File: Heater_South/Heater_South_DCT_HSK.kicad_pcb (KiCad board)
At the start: 2 copper layers, 52.1 x 57.1 mm, 8 parts, among them J1 NHB1, J2 NHB2, J3 Heater North

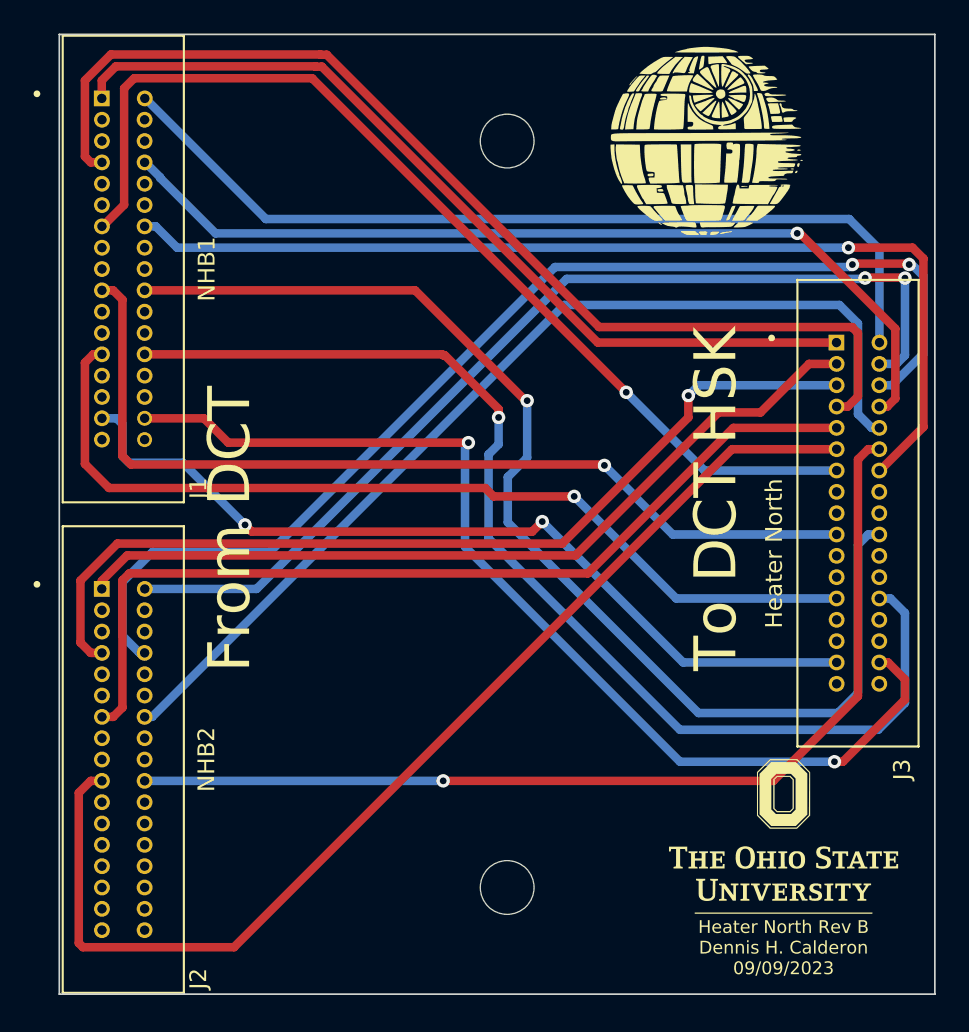
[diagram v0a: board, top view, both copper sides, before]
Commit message: Updated Heater North and Heater South boards.
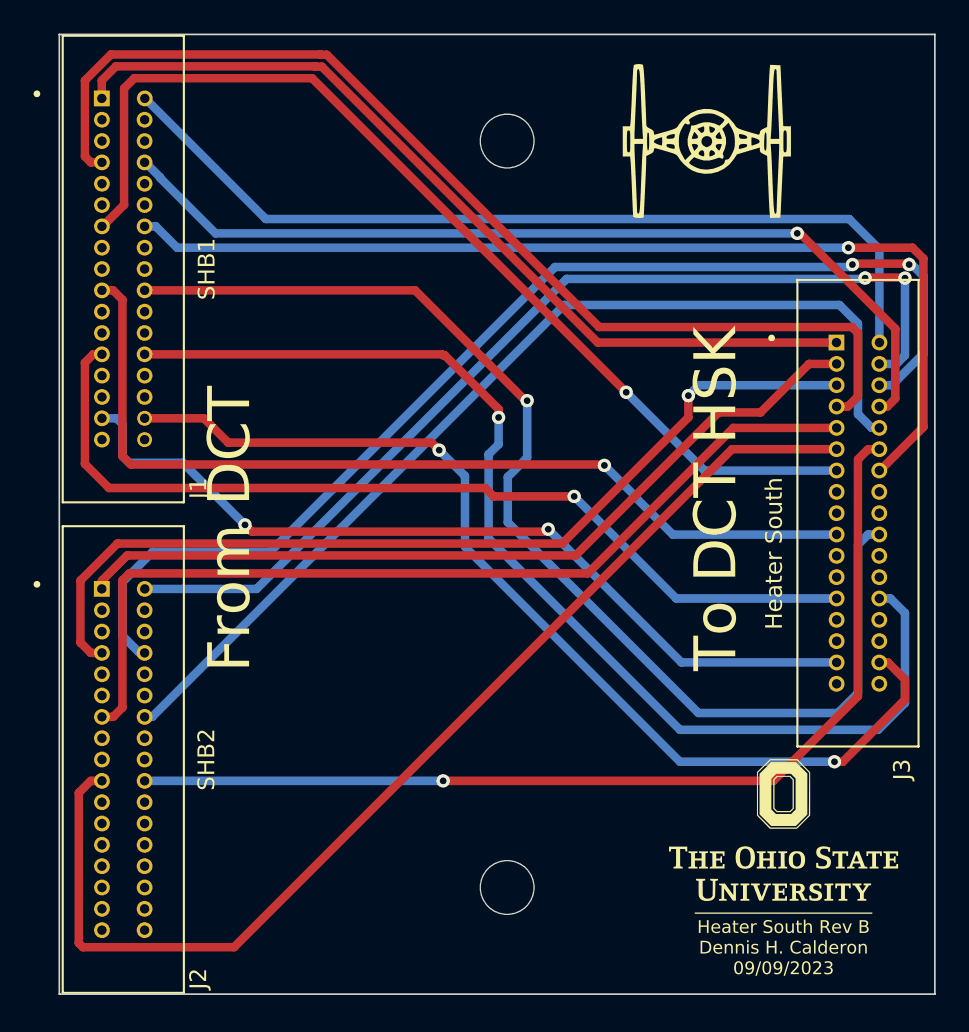
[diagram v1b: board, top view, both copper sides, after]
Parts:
- J1: value NHB1 -> SHB1
- J2: value NHB2 -> SHB2
- J3: value Heater North -> Heater South
- moved G*** 0.43 mm to (130.0, 53.4)
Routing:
- net /HB1_32: track 62.3 -> 60.9 mm
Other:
- board text added: "Heater South Rev B Dennis H. Calderon 09/09/2023"
- board text added: "South"
- board text removed: "Heater North Rev B Dennis H. Calderon 09/09/2023"
- board text removed: "North"
